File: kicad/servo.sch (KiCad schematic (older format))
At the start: 0 parts

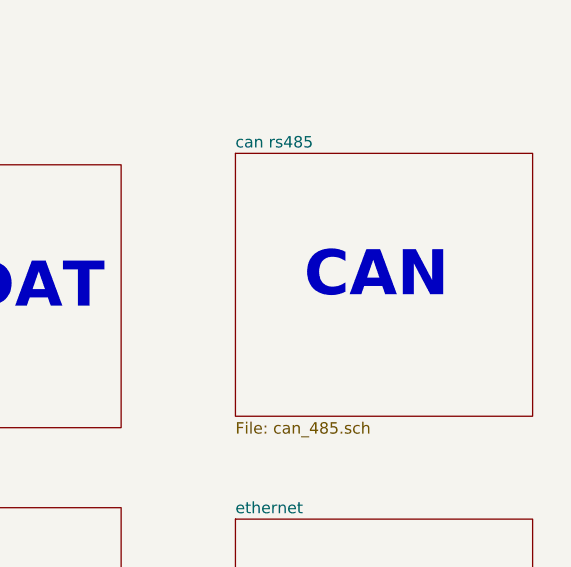
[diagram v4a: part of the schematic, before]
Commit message: added some 3d models, elminating 15vc and 2 lems
I've elminated 15vc 'cause I don't use these voltage, so I'd change 20w
15v heating power to 10w 5v more efficiency voltage to drive 3.3 and
1.2v to the core and logic. I've also elminated 2 LEMS 'cause space..
even thought there remain 3 for each motor.. more than necesary...keep
going
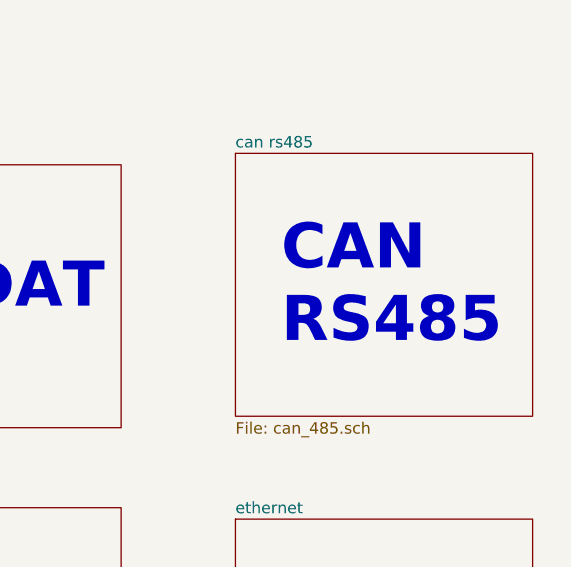
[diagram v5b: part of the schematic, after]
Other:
- note added: "CAN\nRS485"
- note removed: "CAN"
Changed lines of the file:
@@
 F1 "can_485.sch" 50
 $EndSheet
-Text Notes 12650 4500 0    197  ~ 39
-CAN
+Text Notes 12550 4700 0    197  ~ 39
+CAN\nRS485
 $Sheet
 S 7050 2400 1300 1150

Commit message: I forgot that QUEP was diferential!! all to back....
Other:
- note added: "STEP\nDIR\n"
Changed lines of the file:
@@
 $Descr A3 16535 11693
 encoding utf-8
-Sheet 1 18
+Sheet 1 19
 Title "servo drive"
 Date "2020-01-09"
@@
 Text Notes 7300 4900 0    197  ~ 39
 uC\nCLK\nDbg
-Text Notes 10750 4550 0    197  ~ 39
-ENDAT
+Text Notes 10850 4750 0    197  ~ 39
+STEP\nDIR\n
 $Sheet
 S 10550 3900 1300 1150
 U 5DE3DF56
-F0 "endat" 50
-F1 "endat.sch" 50
+F0 "step_dir" 50
+F1 "step_dir.sch" 50
 $EndSheet
 $Sheet
@@
 Text Notes 3700 3050 0    197  ~ 39
 SDELTA\n
+Text Notes 10750 2950 0    197  ~ 39
+ENDAT
+$Sheet
+S 10550 2300 1300 1150
+U 5F8D42C2
+F0 "sheet5F8D42BF" 50
+F1 "endat.sch" 50
+$EndSheet
 $EndSCHEMATC

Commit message: placing smmall capacitors and resistors nerar his group
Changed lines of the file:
@@
 S 10550 2300 1300 1150
 U 5F8D42C2
-F0 "sheet5F8D42BF" 50
+F0 "endat" 50
 F1 "endat.sch" 50
 $EndSheet

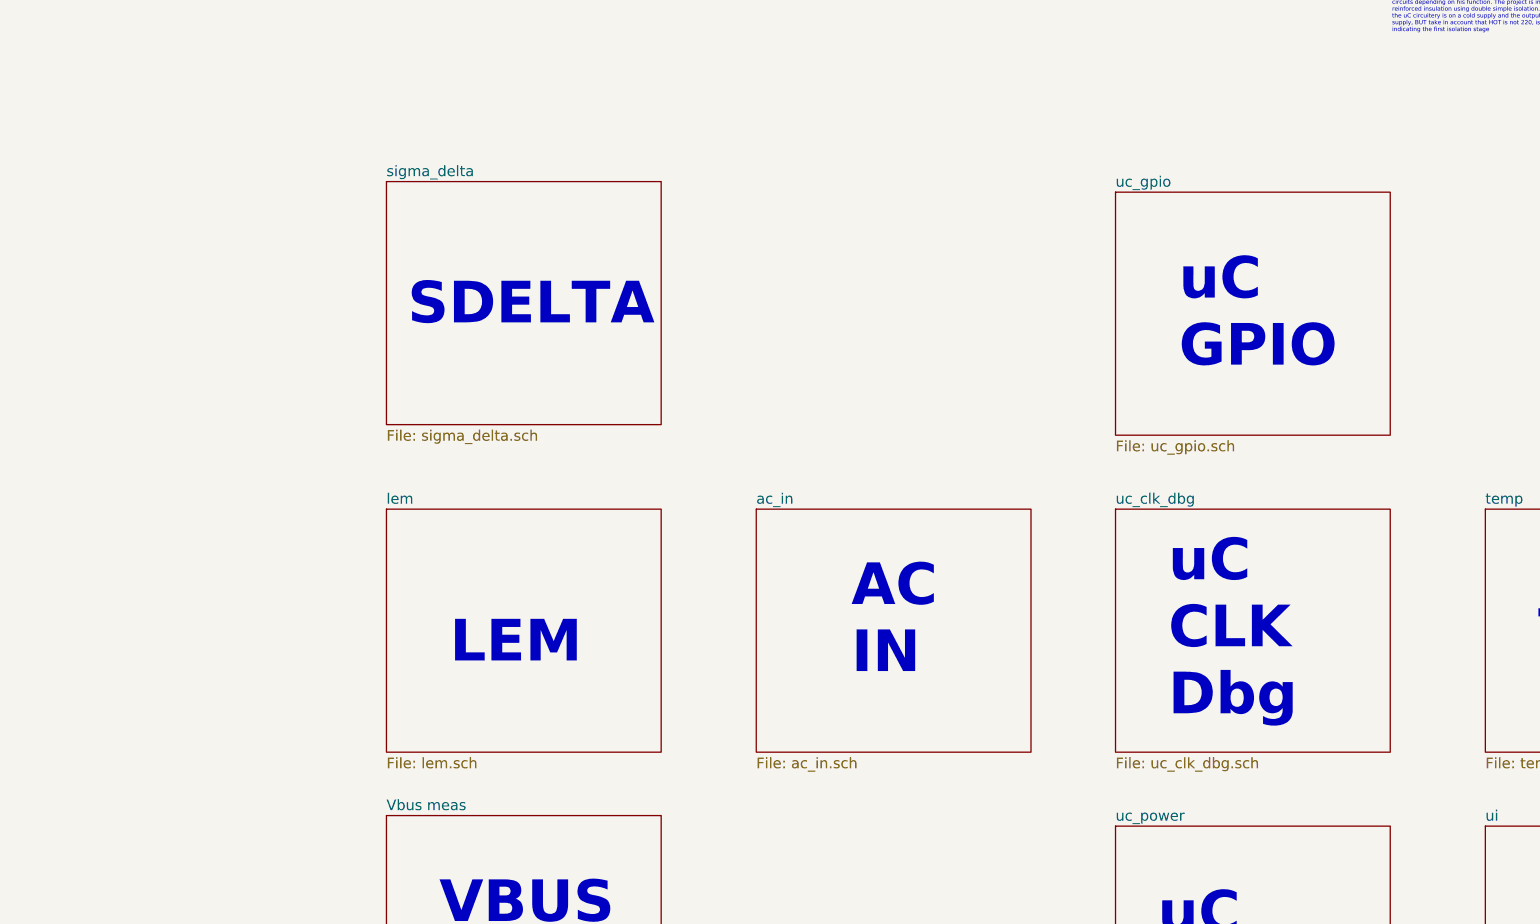
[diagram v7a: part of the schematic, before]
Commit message: change in 5v interface scenario.. remove bridges
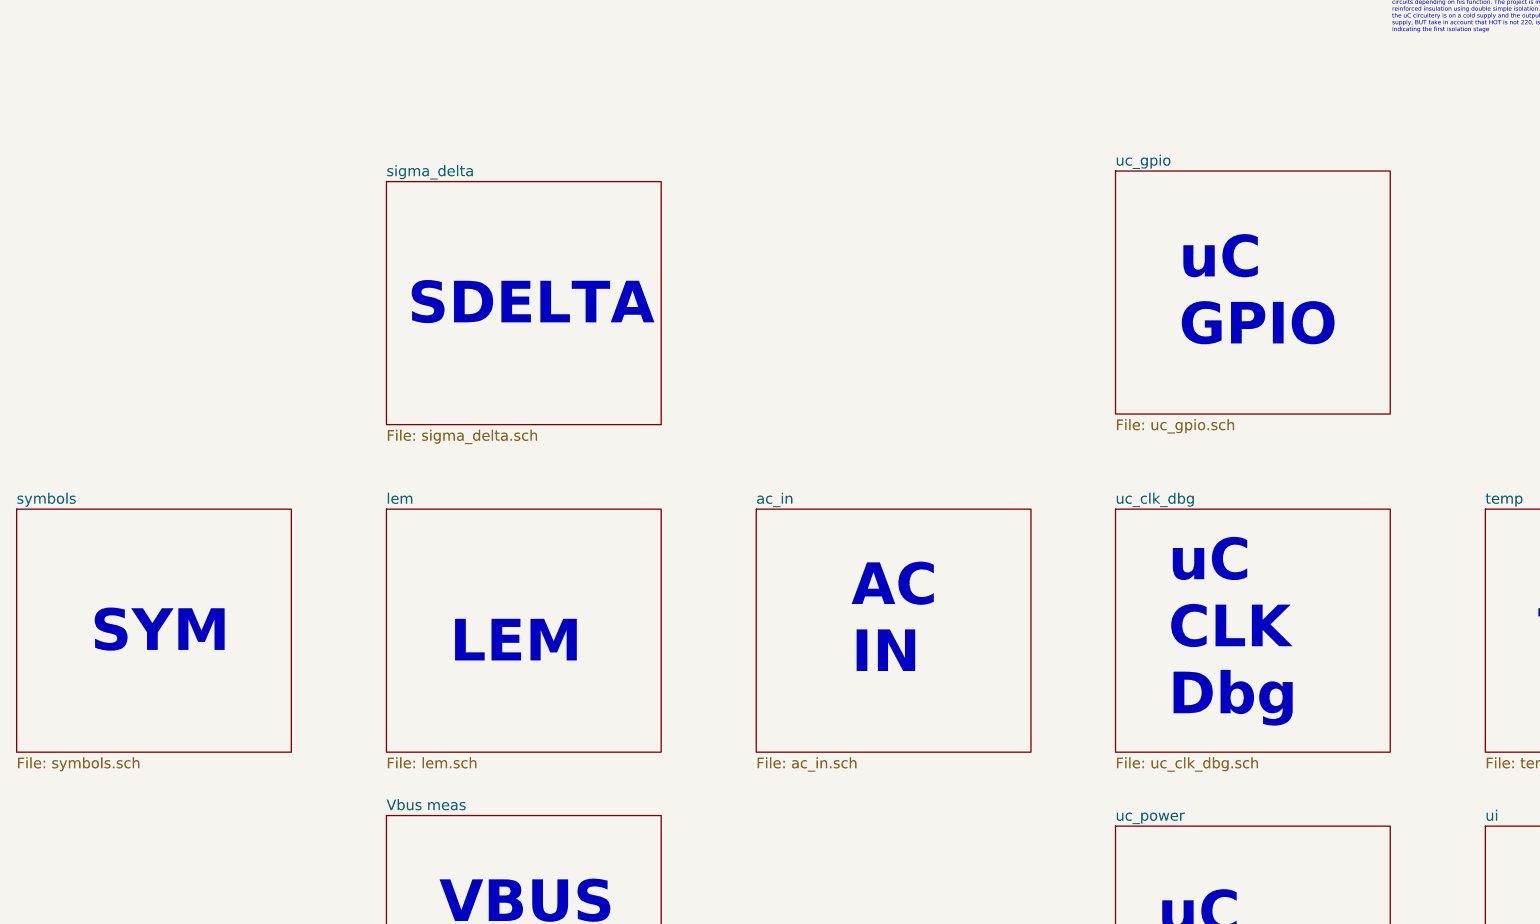
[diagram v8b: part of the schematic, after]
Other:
- note added: "SYM\n"
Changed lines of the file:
@@
 $Descr A3 16535 11693
 encoding utf-8
-Sheet 1 19
+Sheet 1 20
 Title "servo drive"
 Date "2020-01-09"
@@
 CAN\nRS485
 $Sheet
-S 7050 2400 1300 1150
+S 1850 3900 1300 1150
 U 5E033FE4
-F0 "uc_gpio" 50
-F1 "uc_gpio.sch" 50
+F0 "symbols" 50
+F1 "symbols.sch" 50
 $EndSheet
-Text Notes 7350 3250 0    197  ~ 39
-uC\nGPIO
+Text Notes 2200 4600 0    197  ~ 39
+SYM\n
 $Sheet
 S 8800 5400 1300 1150
@@
 F1 "endat.sch" 50
 $EndSheet
+$Sheet
+S 7050 2300 1300 1150
+U 5ED1E8B7
+F0 "uc_gpio" 50
+F1 "uc_gpio.sch" 50
+$EndSheet
+Text Notes 7350 3150 0    197  ~ 39
+uC\nGPIO
 $EndSCHEMATC
